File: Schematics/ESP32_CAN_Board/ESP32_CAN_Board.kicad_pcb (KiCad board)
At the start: 2 copper layers, 23 parts, among them J8 USB_C_Receptacle, U1 SN65HVD230, U7 LDL1117-3.3

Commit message: initial design completed
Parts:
- removed R16, R17: 10k, Resistor_SMD:R_0805_2012Metric_Pad1.20x1.40mm_HandSolder
- added D21: SRV05-4.TCT, myFootprints:SOT95P280X145-6N, F.Cu at (129.3, 87.5)
- added J1: Screw_Terminal_01x04, TerminalBlock:TerminalBlock_Xinya_XY308-2.54-4P_1x04_P2.54mm_Horizontal, F.Cu at (104.2, 70.8)
- added J2: Screw_Terminal_01x04, TerminalBlock:TerminalBlock_Xinya_XY308-2.54-4P_1x04_P2.54mm_Horizontal, F.Cu at (104.3, 59.0)
- added J3: Screw_Terminal_01x02, TerminalBlock:TerminalBlock_Xinya_XY308-2.54-2P_1x02_P2.54mm_Horizontal, F.Cu at (104.2, 82.5)
- added PowerIn1: 2 pin Molex, myFootprints:MOLEX_26013114, F.Cu at (113.6, 85.8)
- added REF**: MountingHole_2.2mm_M2_Pad_Via, MountingHole:MountingHole_2.2mm_M2_Pad_Via, F.Cu at (146.0, 96.0)
- added REF**: MountingHole_2.2mm_M2_Pad_Via, MountingHole:MountingHole_2.2mm_M2_Pad_Via, F.Cu at (104.0, 96.0)
- added REF**: MountingHole_2.2mm_M2_Pad_Via, MountingHole:MountingHole_2.2mm_M2_Pad_Via, F.Cu at (146.0, 54.0)
- added REF**: MountingHole_2.2mm_M2_Pad_Via, MountingHole:MountingHole_2.2mm_M2_Pad_Via, F.Cu at (104.0, 54.0)
- added U4: ESP32-C3-MINI-1-N4, myFootprints:XCVR_ESP32-C3-MINI-1-N4, F.Cu at (147.1, 69.7)
- moved C2 40.7 mm to (146.2, 61.5)
- moved C1 40.1 mm to (146.2, 59.3)
- moved R3 31.4 mm to (135.0, 92.1), turned to 90 degrees
- moved J8 21.2 mm to (128.5, 95.5)
- moved R18 19.9 mm to (121.8, 91.9), turned to 90 degrees
- moved JP1 19.8 mm to (136.6, 60.8), turned to -90 degrees
- moved U7 18.5 mm to (127.8, 81.0)
- moved C7 17.5 mm to (124.3, 75.2), turned to 90 degrees
- moved D8 17.0 mm to (118.6, 76.2), turned to 180 degrees
- moved D9 15.6 mm to (120.3, 82.5), turned to -90 degrees
- moved R2 15.4 mm to (133.1, 60.1)
- moved C22 12.3 mm to (133.2, 82.6), turned to -90 degrees
- moved BootSwitch1 10.6 mm to (142.9, 83.8)
- moved R5 9.88 mm to (148.3, 84.5), turned to -90 degrees
- moved RSTSwitch1 9.18 mm to (141.3, 89.7)
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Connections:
- C1 pad 1: /MCU/ESPPower -> +3.3V
- C2 pad 1: /MCU/ESPPower -> +3.3V
- C22 pad 1: /MCU/ESPPower -> +3.3V
- U7 pad 3: /MCU/ESPPower -> +3.3V
- U7 pad 4: /MCU/ESPPower -> +3.3V
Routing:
- net GND: track 0.00 -> 69.9 mm, vias 0 -> 24
- net /MCU/NRST: track 0.00 -> 46.2 mm, vias 0 -> 2
- net Net-(J3-Pin_2): track 0.00 -> 45.9 mm, vias 0 -> 1
- net Net-(J3-Pin_1): track 0.00 -> 44.7 mm, vias 0 -> 1
- net /MCU/Pin6: track 0.00 -> 42.4 mm, vias 0 -> 1
- net Net-(J1-Pin_4): track 0.00 -> 37.4 mm, vias 0 -> 1
- net Net-(J1-Pin_3): track 0.00 -> 36.7 mm, vias 0 -> 1
- net /MCU/Pin12: track 0.00 -> 36.6 mm, vias 0 -> 1
- net /MCU/Pin13: track 0.00 -> 36.6 mm, vias 0 -> 1
- net /MCU/Pin18: track 0.00 -> 36.2 mm, vias 0 -> 1
- net Net-(J1-Pin_2): track 0.00 -> 36.0 mm, vias 0 -> 1
- net /MCU/Pin16: track 0.00 -> 35.8 mm, vias 0 -> 1
- net /CAN/CANL: track 0.00 -> 33.7 mm
- net +3.3V: track 0.00 -> 29.0 mm, vias 0 -> 6
- net /MCU/D-: track 0.00 -> 28.0 mm
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- added copper zone on In2.Cu, net +3.3V
- added copper zone on B.Cu, net GND
- added copper zone on In1.Cu, net GND
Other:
- board outline added: 56 x 50 mm
- copper layers 2 -> 4

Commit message: finished ready for order
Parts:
- added G***: LOGO, LOGO, F.Cu at (131.1, 54.0)
- added PowerLED1: RLED, LED_SMD:LED_0603_1608Metric_Pad1.05x0.95mm_HandSolder, F.Cu at (140.7, 51.9)
- added R1: 27r, Resistor_SMD:R_0805_2012Metric_Pad1.20x1.40mm_HandSolder, F.Cu at (141.3, 79.1)
- added R6: 27r, Resistor_SMD:R_0805_2012Metric_Pad1.20x1.40mm_HandSolder, F.Cu at (136.8, 79.7)
- added R7: 1k, Resistor_SMD:R_0805_2012Metric_Pad1.20x1.40mm_HandSolder, F.Cu at (137.5, 53.0)
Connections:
- D21 pad 1: /MCU/D+ -> /USBC/D+
- D21 pad 6: /MCU/D- -> /USBC/D-
- J8 pad A6: /MCU/D+ -> /USBC/D+
- J8 pad A7: /MCU/D- -> /USBC/D-
- J8 pad B6: /MCU/D+ -> /USBC/D+
- J8 pad B7: /MCU/D- -> /USBC/D-
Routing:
- net /MCU/D+: track 25.2 -> 3.86 mm
- net /USBC/D-: track 0.00 -> 21.0 mm
- net /MCU/D-: track 28.0 -> 6.96 mm
- net /USBC/D+: track 0.00 -> 20.8 mm
- net Net-(PowerLED1-A): track 0.00 -> 2.32 mm
- net GND: track 69.9 -> 71.4 mm, vias 24 -> 25
- net +3.3V: track 29.0 -> 30.5 mm, vias 6 -> 7
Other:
- board text added: "+"
- board text added: "-"
- board text added: "12"
- board text added: "13"
- board text added: "16"
- board text added: "18"
- board text added: "21"
- board text added: "22"
- board text added: "23"
- board text added: "6"
- board text added: "CAN"
- board text added: "Power"
- board text added: "RX"
- board text added: "TX"
- board text added: "made by reed"

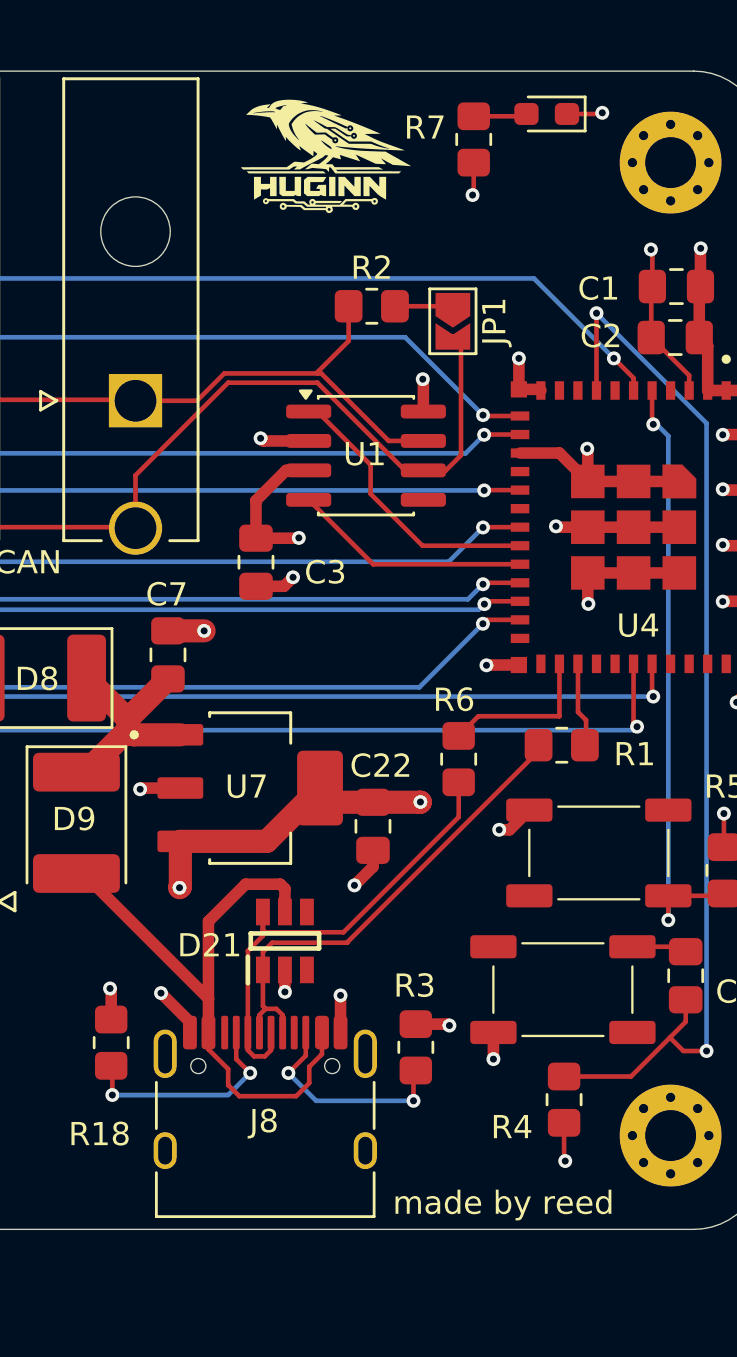
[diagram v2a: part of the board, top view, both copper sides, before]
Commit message: final Draft Completed, In JLPCB Cart
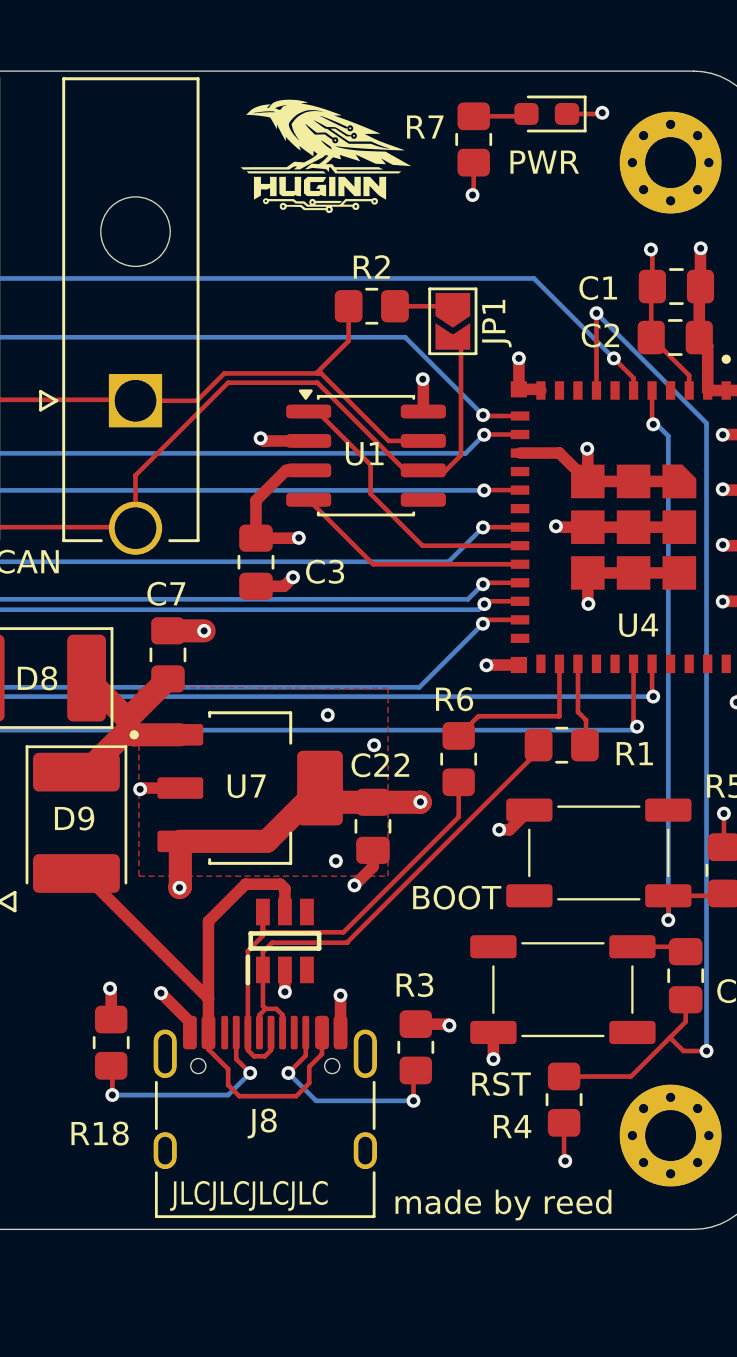
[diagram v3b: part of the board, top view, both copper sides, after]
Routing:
- net GND: vias 25 -> 28
- added copper zone on F.Cu, net GND
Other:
- board text added: "BOOT"
- board text added: "JLCJLCJLCJLC"
- board text added: "PWR"
- board text added: "RST"

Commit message: updated ESPBoard
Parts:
- moved BootSwitch1 0.16 mm to (142.8, 83.6)
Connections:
- BootSwitch1 pad 1: +3.3V -> GND
- R5 pad 1: GND -> +3.3V
- RSTSwitch1 pad 1: unconnected-(RSTSwitch1-Pad1) -> GND
- RSTSwitch1 pad 2: Net-(C8-Pad2) -> unconnected-(RSTSwitch1-Pad2)
- RSTSwitch1 pad 3: GND -> unconnected-(RSTSwitch1-Pad3)
- RSTSwitch1 pad 4: unconnected-(RSTSwitch1-Pad4) -> Net-(C8-Pad2)
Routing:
- net unconnected-(RSTSwitch1-Pad3): track 0.00 -> 1.15 mm, vias 0 -> 1
- net GND: track 71.4 -> 70.5 mm, vias 28 -> 27
